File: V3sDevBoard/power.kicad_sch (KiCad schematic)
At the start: 24 parts, among them U2 SY8089AAAC, U3 SY8089AAAC, U4 SY8089AAAC

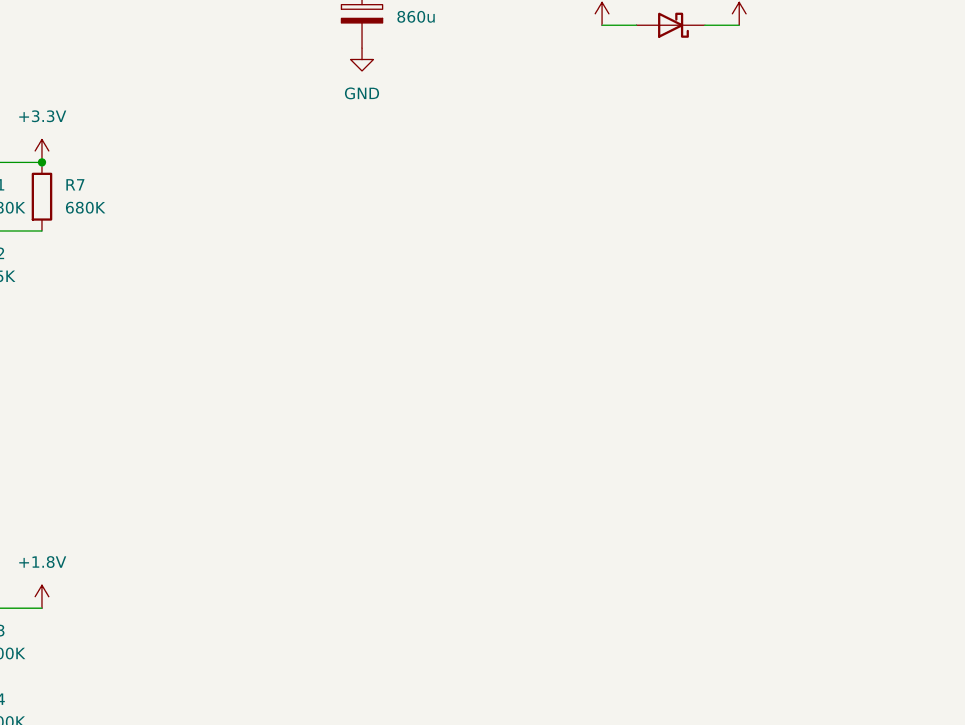
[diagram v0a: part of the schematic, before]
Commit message: drawing schematic
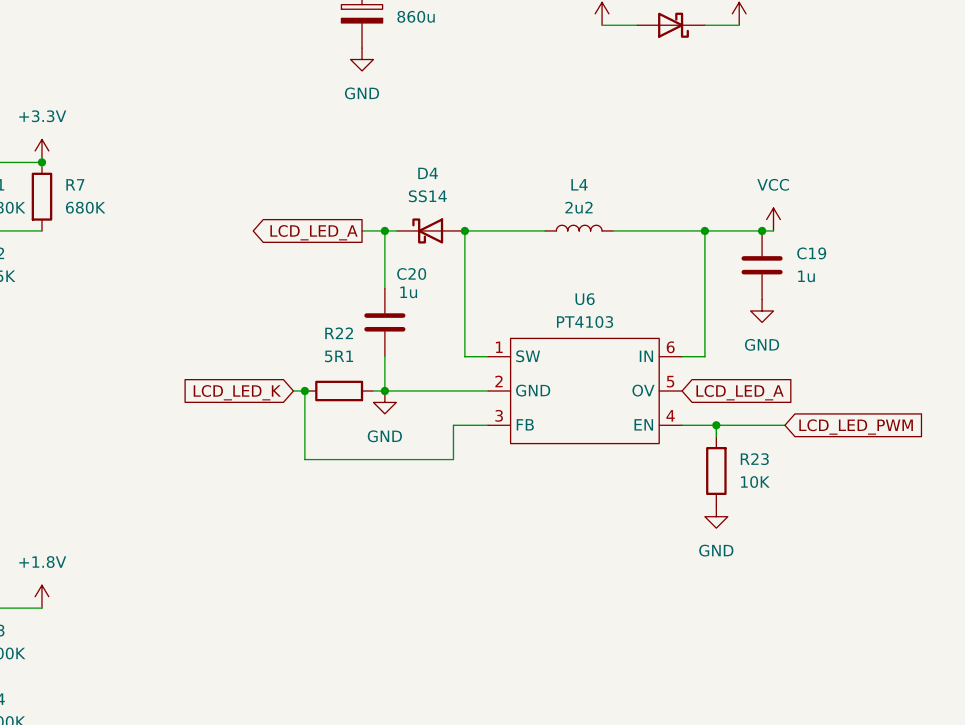
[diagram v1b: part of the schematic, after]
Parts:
- added C19, C20: 1u, Capacitor_SMD:C_0805_2012Metric_Pad1.18x1.45mm_HandSolder, symbol Device:C
- added D4: SS14, Diode_SMD:D_SMA, symbol Diode:SS14
- added L4: 2u2, Inductor_SMD:L_APV_APH0420, symbol Device:L
- added R22: 5R1, Resistor_SMD:R_0805_2012Metric_Pad1.20x1.40mm_HandSolder, symbol Device:R
- added R23: 10K, Resistor_SMD:R_0805_2012Metric_Pad1.20x1.40mm_HandSolder, symbol Device:R
- added U6: PT4103, Package_TO_SOT_SMD:SOT-23-6_Handsoldering, symbol Custom:PT4103
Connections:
- net GND: now also C19.2, C20.2, R22.2, R23.1, U6.2 (GND)
- net VCC: now also C19.1, L4.2, U6.6 (IN)
- new net: D4.2 (A), L4.1, U6.1 (SW)
- new net LCD_LED_A: C20.1, D4.1 (K), U6.5 (OV)
- new net LCD_LED_K: R22.1, U6.3 (FB)
- new net LCD_LED_PWM: R23.2, U6.4 (EN)

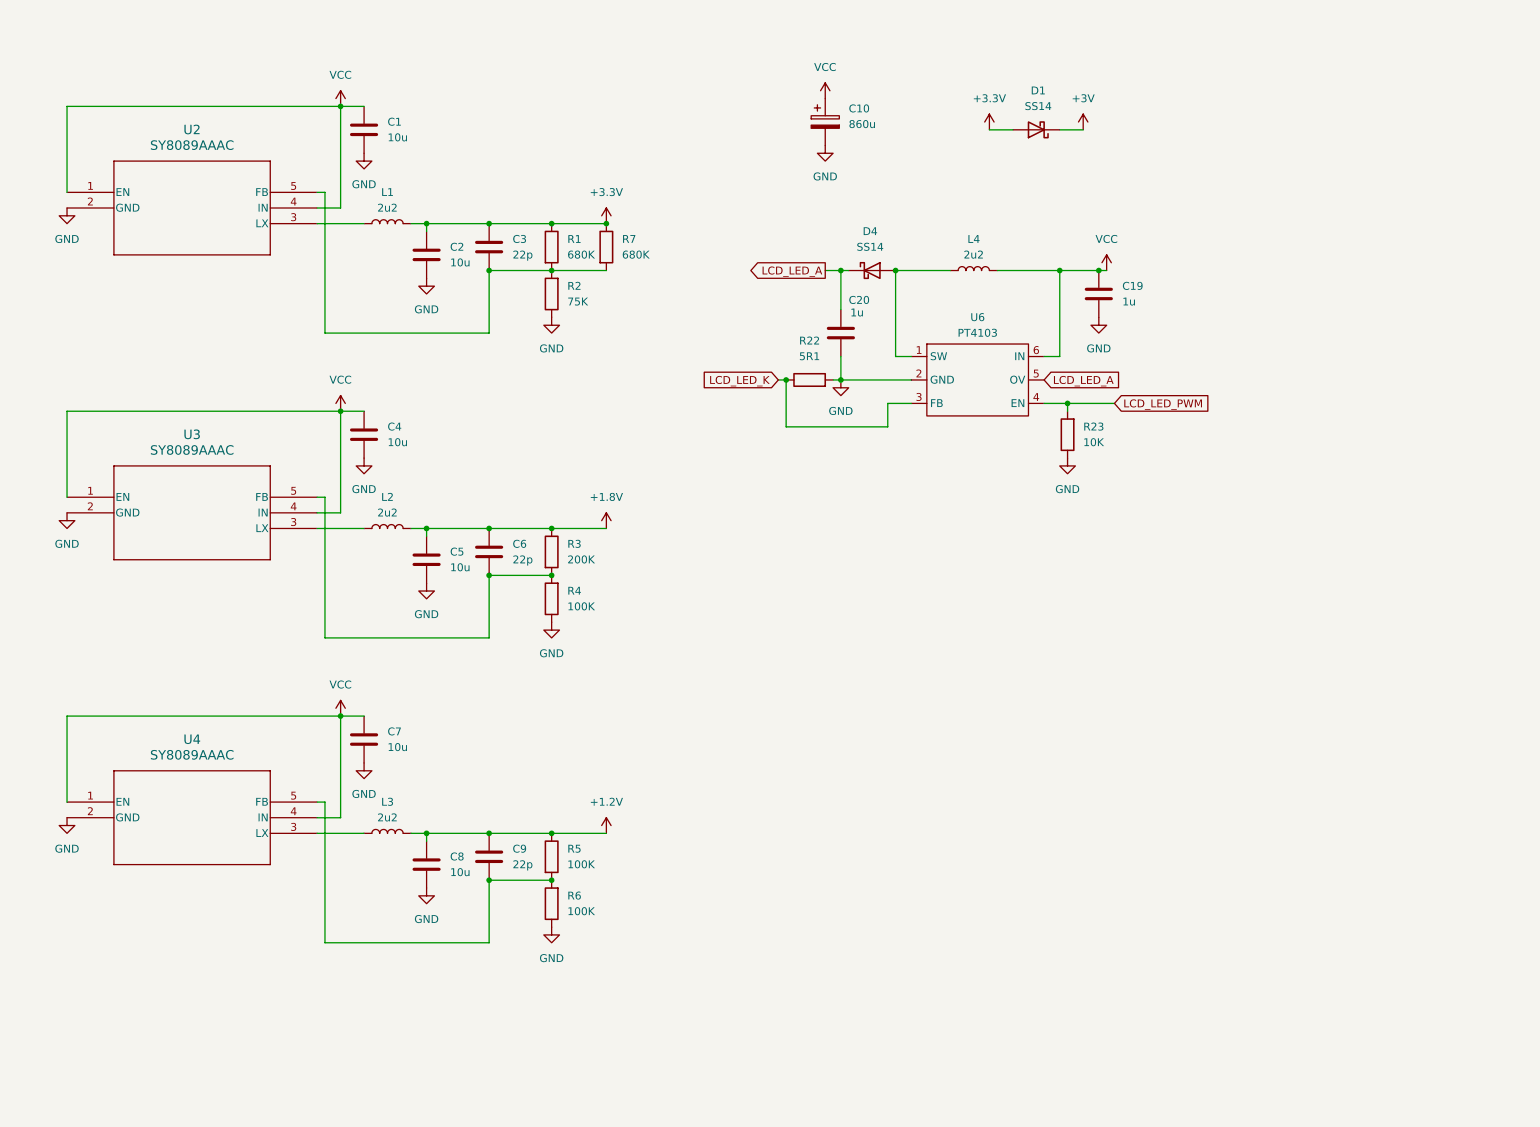
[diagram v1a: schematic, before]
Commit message: drawing schematics
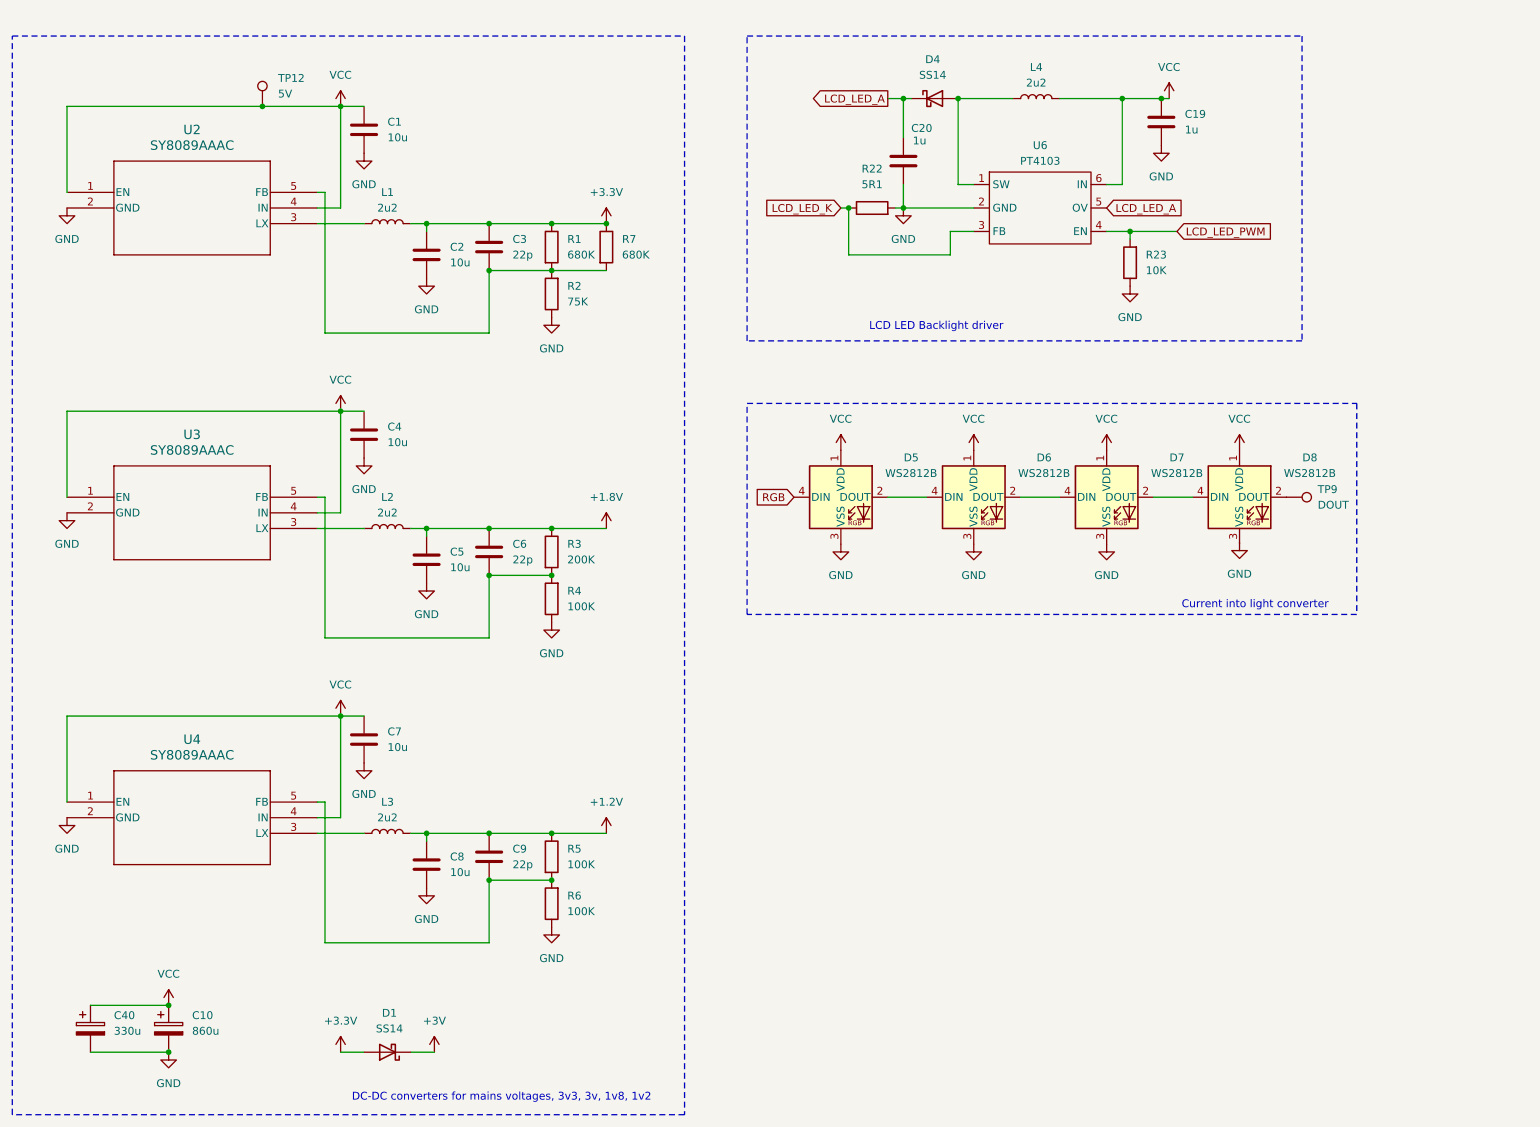
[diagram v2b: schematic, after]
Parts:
- added C40: 330u, Capacitor_Tantalum_SMD:CP_EIA-7343-15_Kemet-W_HandSolder, symbol Device:C_Polarized
- added D5, D6, D7, D8: WS2812B, LED_SMD:LED_WS2812B_PLCC4_5.0x5.0mm_P3.2mm, symbol LED:WS2812B
- added TP12: 5V, TestPoint:TestPoint_Pad_D1.0mm, symbol Connector:TestPoint
- added TP9: DOUT, TestPoint:TestPoint_Pad_D1.0mm, symbol Connector:TestPoint
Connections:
- net GND: now also C40.2, D5.3 (VSS), D6.3 (VSS), D7.3 (VSS)
- net VCC: now also C40.1, D5.1 (VDD), D6.1 (VDD), D7.1 (VDD), D8.1 (VDD), TP12.1
- new net: D5.2 (DOUT), D6.4 (DIN)
- new net: D8.2 (DOUT), TP9.1
- new net: D7.2 (DOUT), D8.4 (DIN)
- new net: D6.2 (DOUT), D7.4 (DIN)
- new net RGB: D5.4 (DIN)
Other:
- note added: "Current into light converter"
- note added: "DC-DC converters for mains voltages, 3v3, 3v, 1v8, 1v2"
- note added: "LCD LED Backlight driver"
- company: (none) -> J.K.
- title: (none) -> V3s Dev Board
- moved on the sheet: C10, C19, C20, D1, D4, L4, R22, R23, U6

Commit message: advancing in schematics and footprints
Making needed custom footprints for connectors, adding a lot of small changes to schematics.
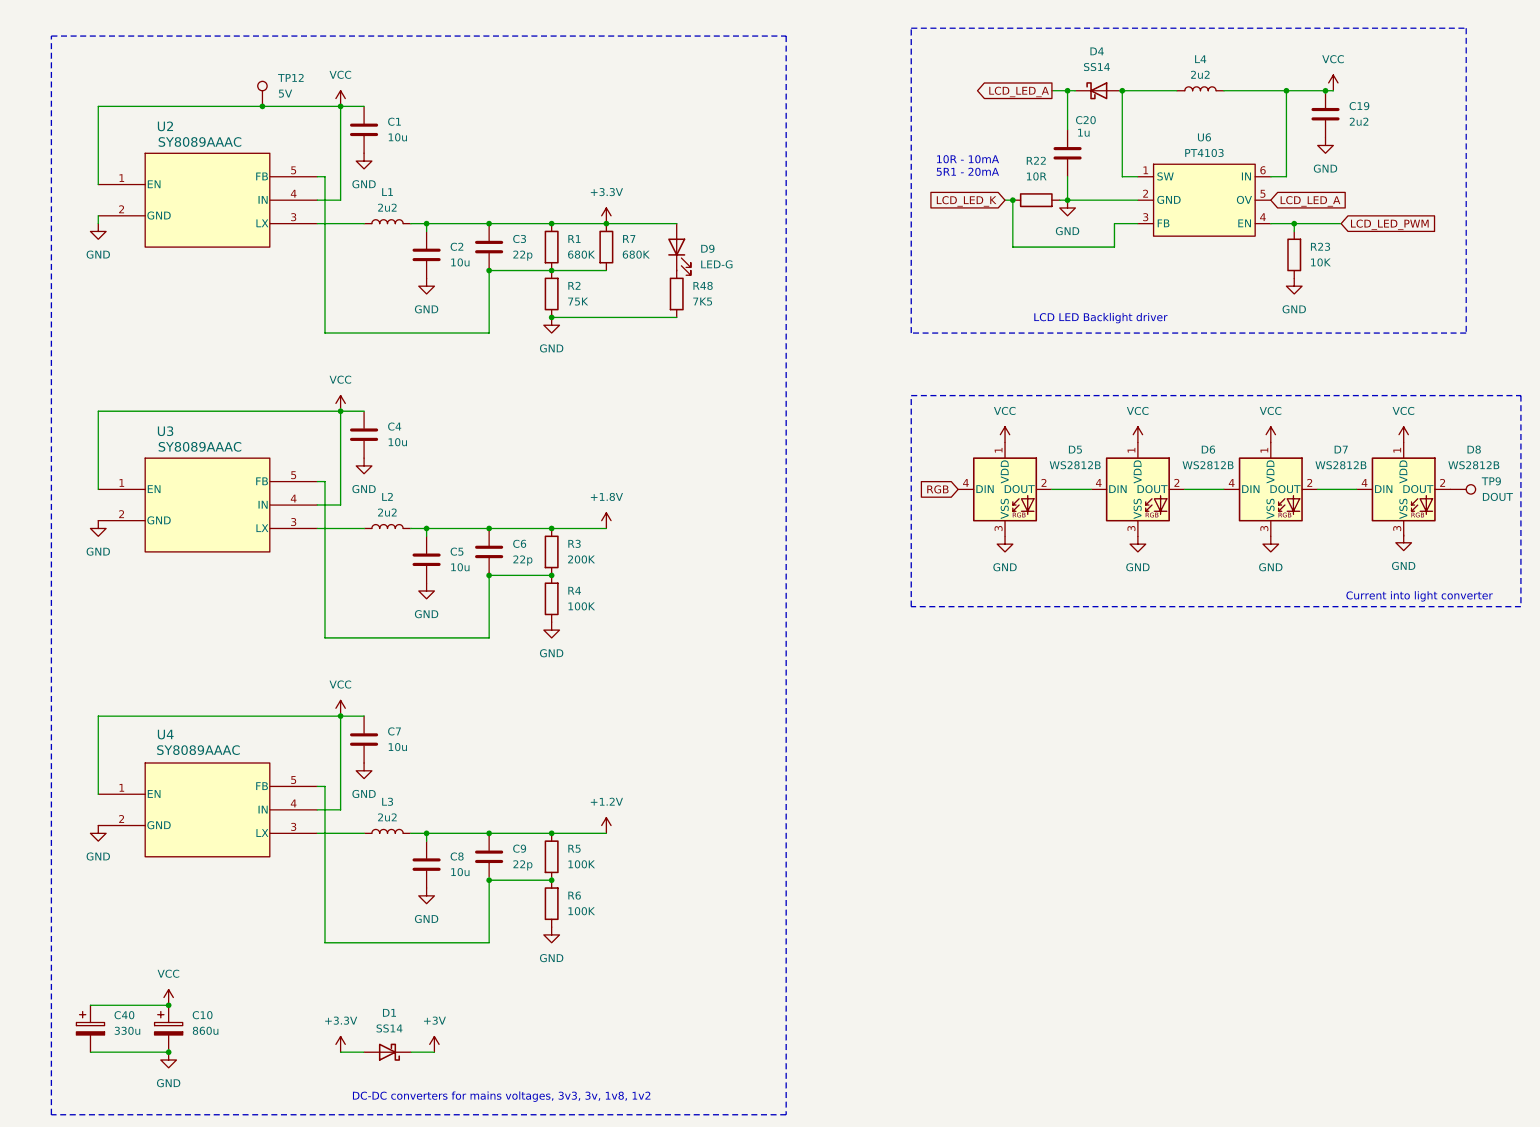
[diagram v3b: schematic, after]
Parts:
- added D9: LED-G, LED_SMD:LED_0805_2012Metric_Pad1.15x1.40mm_HandSolder, symbol Device:LED
- added R48: 7K5, Resistor_SMD:R_0805_2012Metric_Pad1.20x1.40mm_HandSolder, symbol Device:R
- C19: value 1u -> 2u2
- R22: value 5R1 -> 10R
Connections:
- net +3.3V: now also D9.2 (A)
- net GND: now also R48.2
- new net: D9.1 (K), R48.1
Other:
- note added: "10R - 10mA 5R1 - 20mA"
- title: V3s Dev Board -> V3s_Dev_Board
- moved on the sheet: C19, C20, D4, D5, D6, D7, D8, L4, R22, R23, TP9

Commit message: completing schematics
completing schematics, adding netclasses, fixing bugs, updating readme, starting pcb
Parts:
- removed TP12: 5V, TestPoint:TestPoint_Pad_D1.0mm, symbol Connector:TestPoint
- added F1: PCB fuse, Fuse:Fuse_1206_3216Metric, symbol Device:Fuse_Small
- added J10: Power, Connector_PinHeader_2.54mm:PinHeader_1x02_P2.54mm_Vertical, symbol Connector:Conn_01x02_Pin
- added JP4, JP5, JP7: pwr, Jumper:SolderJumper-2_P1.3mm_Bridged_RoundedPad1.0x1.5mm, symbol Jumper:SolderJumper_2_Bridged
- added TP13: RGB1, TestPoint:TestPoint_Pad_D1.0mm, symbol Connector:TestPoint
- added TP14: RGB2, TestPoint:TestPoint_Pad_D1.0mm, symbol Connector:TestPoint
- added TP16: RGB3, TestPoint:TestPoint_Pad_D1.0mm, symbol Connector:TestPoint
- added TP17: RGB4, TestPoint:TestPoint_Pad_D1.0mm, symbol Connector:TestPoint
- C1, C2, C4, C5, C7, C8: footprint Capacitor_SMD:C_0805_2012Metric_Pad1.18x1.45mm_HandSolder -> Capacitor_SMD:C_1206_3216Metric
- C20: value 1u -> 220n
- L1, L2, L3, L4: value 2u2 -> 4u7
- U2, U3, U4: footprint SY8089AAAC_SGY -> footprints:SY8089AAAC_SGY
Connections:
- net GND: now also D8.3 (VSS), J10.2 (Pin_2)
- net RGB: now also TP13.1
- net VCC: now also F1.1, F1.2, J10.1 (Pin_1), JP4.2 (B), JP5.2 (B), JP7.2 (B); no longer C1.1, C4.1, C7.1, U2.1 (EN), U2.4 (IN), U3.1 (EN), U3.4 (IN), U4.1 (EN), U4.4 (IN)
- net at D5.2 (DOUT), D6.4 (DIN): now also TP14.1
- net at D7.2 (DOUT), D8.4 (DIN): now also TP17.1
- net at D6.2 (DOUT), D7.4 (DIN): now also TP16.1
- new net: C7.1, JP5.1 (A), U4.1 (EN), U4.4 (IN)
- new net: C1.1, JP7.1 (A), U2.1 (EN), U2.4 (IN)
- new net: C4.1, JP4.1 (A), U3.1 (EN), U3.4 (IN)
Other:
- note added: "DC-DC"
- note added: "LCD LED Backlight"
- note added: "PCB Backlight RGB"
- note removed: "Current into light converter"
- note removed: "DC-DC converters for mains voltages, 3v3, 3v, 1v8, 1v2"
- note removed: "LCD LED Backlight driver"
- company: J.K. -> jakub.kmiecik@protonmail.com
- moved on the sheet: C10, C40, D1
